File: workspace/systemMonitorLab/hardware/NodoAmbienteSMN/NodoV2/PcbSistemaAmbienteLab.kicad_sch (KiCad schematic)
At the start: 0 parts

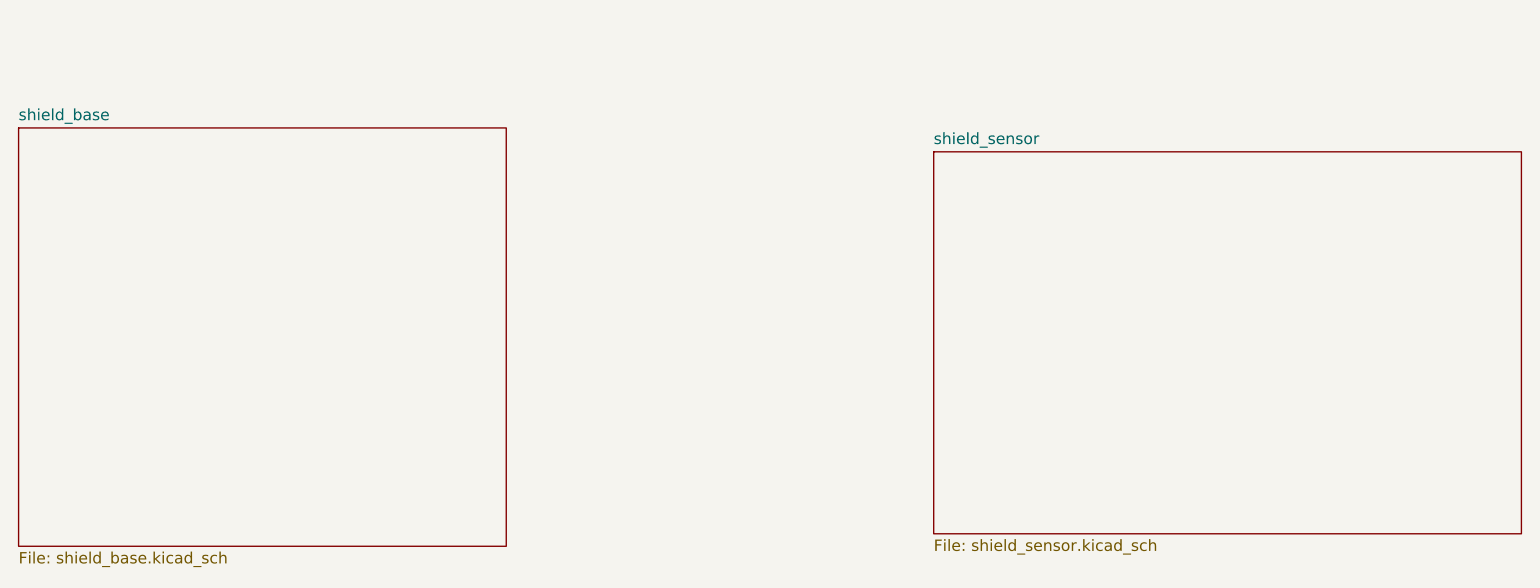
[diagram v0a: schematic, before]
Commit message: Se agregan leds de estado con sus respectivos conectores y se agrega en el codigo la configuracion de los GPIO para usar estos leds como indicadores de envio de datos, conexion con el servidor Web Socket y conectividad wifi
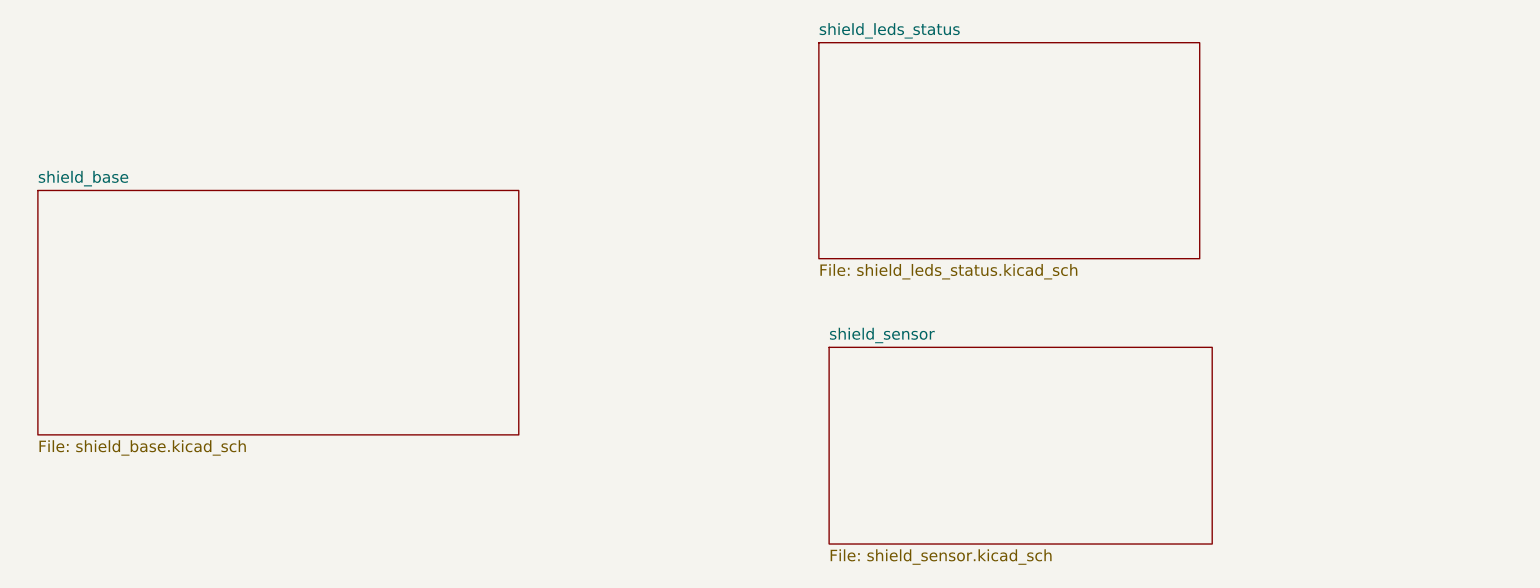
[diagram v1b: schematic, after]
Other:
- added sheet shield_leds_status (shield_leds_status.kicad_sch)
